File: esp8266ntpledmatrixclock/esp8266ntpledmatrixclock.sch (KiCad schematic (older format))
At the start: 4 parts, among them J1 Conn_01x05_Male, U1 WeMos_D1_mini

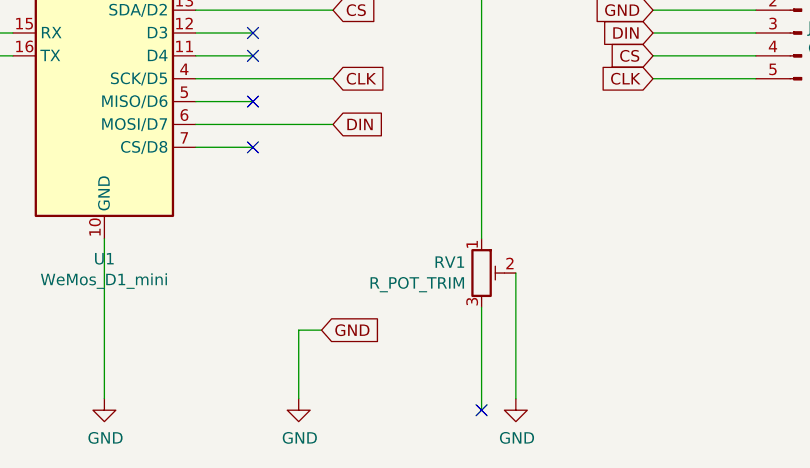
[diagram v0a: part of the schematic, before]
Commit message: added value for resistor in voltage divider measuring ambient light
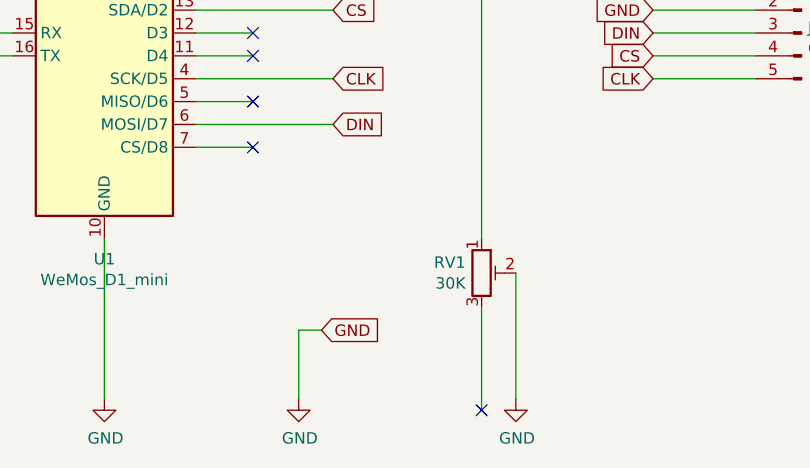
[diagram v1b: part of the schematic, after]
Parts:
- RV1: value R_POT_TRIM -> 30K
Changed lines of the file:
@@
 EESchema Schematic File Version 4
+LIBS:esp8266ntpledmatrixclock-cache
 EELAYER 30 0
 EELAYER END
@@
 P 6550 3500
 F 0 "RV1" H 6480 3546 50  0000 R CNN
-F 1 "R_POT_TRIM" H 6480 3455 50  0000 R CNN
+F 1 "30K" H 6480 3455 50  0000 R CNN
 F 2 "Potentiometer_THT:Potentiometer_Bourns_3386F_Vertical" H 6550 3500 50  0001 C CNN
 F 3 "~" H 6550 3500 50  0001 C CNN
